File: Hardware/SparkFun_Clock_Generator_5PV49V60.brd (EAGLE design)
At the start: 27.9 x 25.4 mm, 74 parts, among them J1 QWIIC_RIGHT_ANGLE, J2 QWIIC_RIGHT_ANGLE, U1 IDT_5P49V60_CLOCK_GENERATOR, Y1 16MHz

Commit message: Update ferrite bead
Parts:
- FB1: value FERRITE_BEAD -> FERRITE_BEAD-120_OHM-0402
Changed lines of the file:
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@@
 <attribute name="VALUE" x="16.4846" y="10.033" size="0.6096" layer="27" font="vector" ratio="20" rot="R270" align="top-center"/>
 </element>
-<element name="FB1" library="SparkFun-Coils" package="0402" value="FERRITE_BEAD" x="18.6436" y="12.827" smashed="yes" rot="R180">
+<element name="FB1" library="SparkFun-Coils" package="0402" value="FERRITE_BEAD-120_OHM-0402" x="18.6436" y="12.827" smashed="yes" rot="R180">
+<attribute name="MFG_PART" value="BLM15HB121SN1D" x="18.6436" y="12.827" size="1.778" layer="27" rot="R180" display="off"/>
 <attribute name="NAME" x="18.6436" y="12.065" size="0.6096" layer="25" font="vector" ratio="20" rot="R180" align="bottom-center"/>
-<attribute name="VALUE" x="18.6436" y="13.589" size="0.6096" layer="27" font="vector" ratio="20" rot="R180" align="top-center"/>
+<attribute name="PROD_ID" value="NDUC-14206" x="18.6436" y="12.827" size="1.778" layer="27" rot="R180" display="off"/>
 </element>
 <element name="Y1" library="SparkFun-Clocks" package="CRYSTAL-SMD-2X2.5MM" value="16MHz" x="13.7414" y="19.0246" smashed="yes" rot="R180">

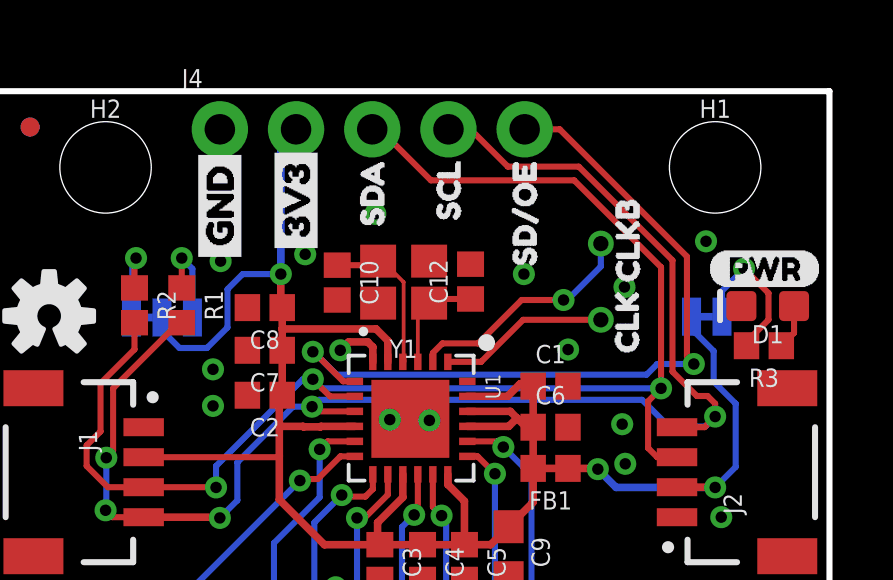
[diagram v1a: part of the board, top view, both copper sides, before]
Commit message: Updates crystal footprint, and fixes routing
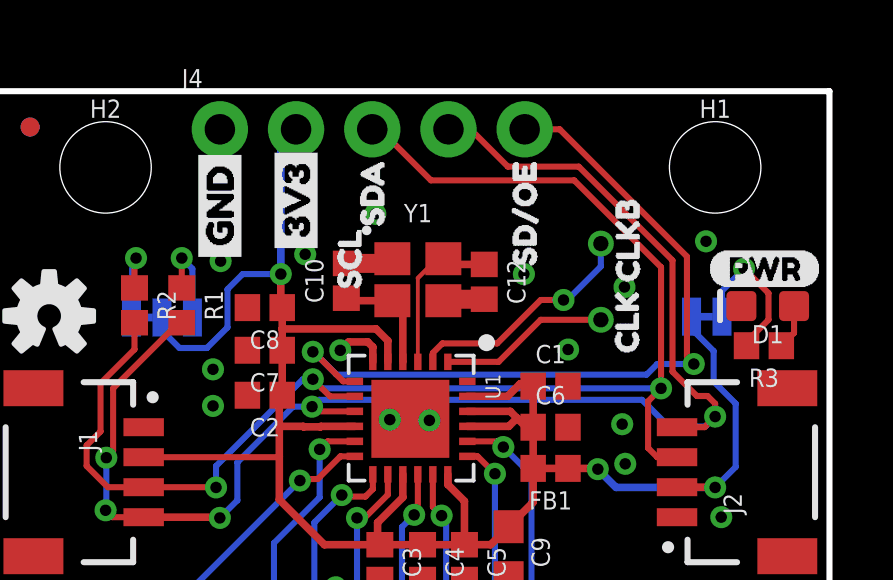
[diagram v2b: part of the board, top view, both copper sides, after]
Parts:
- moved U$6 4.02 mm to (11.9, 18.1)
- moved Y1 0.49 mm to (14.2, 19.1), turned to 0 degrees
- moved C12 0.46 mm to (16.4, 19.0), turned to 270 degrees
- moved C10 0.31 mm to (11.8, 19.1), turned to 90 degrees
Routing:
- net GND: track 42.4 -> 45.4 mm
- net N$2: track 3.55 -> 5.35 mm
- net N$6: track 5.23 -> 3.79 mm
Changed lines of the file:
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@@
 <layer number="37" name="tTest" color="7" fill="1" visible="no" active="yes"/>
 <layer number="38" name="bTest" color="7" fill="1" visible="no" active="yes"/>
-<layer number="39" name="tKeepout" color="4" fill="11" visible="no" active="yes"/>
+<layer number="39" name="tKeepout" color="4" fill="11" visible="yes" active="yes"/>
 <layer number="40" name="bKeepout" color="1" fill="11" visible="no" active="yes"/>
 <layer number="41" name="tRestrict" color="4" fill="10" visible="no" active="yes"/>
@@
 <attribute name="PROD_ID" value="NDUC-14206" x="18.6436" y="12.827" size="1.778" layer="27" rot="R180" display="off"/>
 </element>
-<element name="Y1" library="SparkFun-Clocks" package="CRYSTAL-SMD-2X2.5MM" value="16MHz" x="13.7414" y="19.0246" smashed="yes" rot="R180">
-<attribute name="NAME" x="13.7414" y="17.1196" size="0.6096" layer="25" font="vector" ratio="20" rot="R180" align="bottom-center"/>
-<attribute name="PROD_ID" value="XTAL-14664" x="13.7414" y="19.0246" size="1.778" layer="27" rot="R180" display="off"/>
-<attribute name="VALUE" value="16MHz" x="13.7414" y="19.0246" size="1.778" layer="27" rot="R180" display="off"/>
-</element>
-<element name="C12" library="SparkFun-Capacitors" package="0402" value="12pF" x="15.9766" y="19.0542" smashed="yes" rot="R90">
-<attribute name="NAME" x="15.2146" y="19.0542" size="0.6096" layer="25" font="vector" ratio="20" rot="R90" align="bottom-center"/>
-<attribute name="PROD_ID" value="CAP-14665" x="15.9766" y="19.0542" size="1.778" layer="27" font="vector" rot="R90" display="off"/>
-<attribute name="VALUE" value="12pF" x="16.7386" y="19.0542" size="0.6096" layer="27" font="vector" ratio="20" rot="R90" align="top-center"/>
-</element>
-<element name="C10" library="SparkFun-Capacitors" package="0402" value="12pF" x="11.5316" y="19.0204" smashed="yes" rot="R270">
-<attribute name="NAME" x="12.2936" y="19.0204" size="0.6096" layer="25" font="vector" ratio="20" rot="R270" align="bottom-center"/>
-<attribute name="PROD_ID" value="CAP-14665" x="11.5316" y="19.0204" size="1.778" layer="27" font="vector" rot="R270" display="off"/>
-<attribute name="VALUE" value="12pF" x="10.7696" y="19.0204" size="0.6096" layer="27" font="vector" ratio="20" rot="R270" align="top-center"/>
+<element name="Y1" library="SparkFun-Clocks" package="CRYSTAL-SMD-2X2.5MM" value="16MHz" x="14.224" y="19.1262" smashed="yes">
+<attribute name="NAME" x="14.224" y="21.0312" size="0.6096" layer="25" font="vector" ratio="20" align="bottom-center"/>
+<attribute name="PROD_ID" value="XTAL-14664" x="14.224" y="19.1262" size="1.778" layer="27" display="off"/>
+<attribute name="VALUE" value="16MHz" x="14.224" y="19.1262" size="1.778" layer="27" display="off"/>
+</element>
+<element name="C12" library="SparkFun-Capacitors" package="0402" value="12pF" x="16.4338" y="19.0458" smashed="yes" rot="R270">
+<attribute name="NAME" x="17.1958" y="19.0458" size="0.6096" layer="25" font="vector" ratio="20" rot="R270" align="bottom-center"/>
+<attribute name="PROD_ID" value="CAP-14665" x="16.4338" y="19.0458" size="1.778" layer="27" font="vector" rot="R270" display="off"/>
+<attribute name="VALUE" value="12pF" x="15.6718" y="19.0458" size="0.6096" layer="27" font="vector" ratio="20" rot="R270" align="top-center"/>
+</element>
+<element name="C10" library="SparkFun-Capacitors" package="0402" value="12pF" x="11.8364" y="19.0796" smashed="yes" rot="R90">
+<attribute name="NAME" x="11.0744" y="19.0796" size="0.6096" layer="25" font="vector" ratio="20" rot="R90" align="bottom-center"/>
+<attribute name="PROD_ID" value="CAP-14665" x="11.8364" y="19.0796" size="1.778" layer="27" font="vector" rot="R90" display="off"/>
+<attribute name="VALUE" value="12pF" x="12.5984" y="19.0796" size="0.6096" layer="27" font="vector" ratio="20" rot="R90" align="top-center"/>
 </element>
 <element name="D1" library="SparkFun-LED" package="LED-0603" value="RED" x="25.8826" y="18.2372" smashed="yes" rot="R180">
@@
 <element name="U$4" library="Labels" package="PWR-()-03" value="" x="23.9014" y="19.4818" smashed="yes"/>
 <element name="U$5" library="Every Label" package="SDA11" value="" x="12.7" y="20.2184" smashed="yes" rot="R90"/>
-<element name="U$6" library="Every Label" package="SCL10" value="" x="15.24" y="20.4216" smashed="yes" rot="R90"/>
+<element name="U$6" library="Every Label" package="SCL10" value="" x="11.938" y="18.1356" smashed="yes" rot="R90"/>
 <element name="U$7" library="Every Label" package="SD#OE12" value="" x="17.78" y="18.8976" smashed="yes" rot="R90"/>
 <element name="U$16" library="Every Label" package="CLOCK_GENERATOR0" value="" x="20.447" y="13.2842" smashed="yes" rot="MR0"/>
@@
 <wire x1="11.9126" y1="17.0434" x2="11.6332" y2="16.764" width="0.254" layer="1"/>
 <via x="23.8252" y="20.3962" extent="1-16" drill="0.381"/>
-<contactref element="Y1" pad="P2"/>
-<contactref element="Y1" pad="P4"/>
-<contactref element="C10" pad="2"/>
-<contactref element="C12" pad="2"/>
 <contactref element="D1" pad="C"/>
 <via x="7.8486" y="8.2296" extent="1-16" drill="0.381"/>
@@
 <via x="19.2278" y="16.7894" extent="1-16" drill="0.381"/>
 <via x="10.4648" y="19.9644" extent="1-16" drill="0.381"/>
+<contactref element="Y1" pad="P2"/>
+<contactref element="Y1" pad="P4"/>
+<contactref element="C10" pad="2"/>
+<contactref element="C12" pad="2"/>
+<wire x1="13.37" y1="19.8162" x2="13.2134" y2="19.6596" width="0.635" layer="1"/>
+<wire x1="13.2134" y1="19.6596" x2="11.8364" y2="19.6596" width="0.635" layer="1"/>
+<wire x1="15.07" y1="18.4162" x2="15.1196" y2="18.4658" width="0.635" layer="1"/>
+<wire x1="15.1196" y1="18.4658" x2="16.4338" y2="18.4658" width="0.635" layer="1"/>
 </signal>
 <signal name="3.3V">
@@
 <signal name="CLKIN">
 <contactref element="U1" pad="P1"/>
-<wire x1="15.22" y1="16.378" x2="16.3272" y2="16.378" width="0.2032" layer="1"/>
-<wire x1="16.3272" y1="16.378" x2="17.7292" y2="17.78" width="0.2032" layer="1"/>
+<wire x1="15.22" y1="16.378" x2="16.9114" y2="16.378" width="0.2032" layer="1"/>
+<wire x1="16.9114" y1="16.378" x2="18.3134" y2="17.78" width="0.2032" layer="1"/>
 <contactref element="J8" pad="P$1"/>
-<wire x1="17.7292" y1="17.78" x2="20.32" y2="17.78" width="0.2032" layer="1"/>
+<wire x1="18.3134" y1="17.78" x2="20.32" y2="17.78" width="0.2032" layer="1"/>
 </signal>
 <signal name="CLKINB">
 <contactref element="U1" pad="P2"/>
-<wire x1="15.0368" y1="16.9926" x2="16.2306" y2="16.9926" width="0.2032" layer="1"/>
+<wire x1="15.0368" y1="16.9926" x2="16.8656" y2="16.9926" width="0.2032" layer="1"/>
 <wire x1="14.72" y1="16.6758" x2="14.72" y2="16.378" width="0.2032" layer="1"/>
 <wire x1="15.0368" y1="16.9926" x2="14.72" y2="16.6758" width="0.2032" layer="1"/>
 <contactref element="J7" pad="P$1"/>
-<wire x1="16.2306" y1="16.9926" x2="17.6784" y2="18.4404" width="0.2032" layer="1"/>
-<wire x1="17.6784" y1="18.4404" x2="19.0754" y2="18.4404" width="0.2032" layer="1"/>
+<wire x1="16.8656" y1="16.9926" x2="18.3134" y2="18.4404" width="0.2032" layer="1"/>
+<wire x1="18.3134" y1="18.4404" x2="19.0754" y2="18.4404" width="0.2032" layer="1"/>
 <via x="19.0754" y="18.4404" extent="1-16" drill="0.381"/>
 <wire x1="20.32" y1="20.32" x2="20.32" y2="19.558" width="0.2032" layer="16"/>
@@
 <signal name="N$6">
 <contactref element="U1" pad="P4"/>
+<contactref element="C10" pad="1"/>
+<wire x1="13.72" y1="16.378" x2="13.7454" y2="16.4034" width="0.2032" layer="1"/>
 <contactref element="Y1" pad="P3"/>
-<contactref element="C10" pad="1"/>
-<wire x1="13.7454" y1="19.037" x2="13.0478" y2="19.7346" width="0.127" layer="1"/>
-<wire x1="13.0478" y1="19.7346" x2="12.8954" y2="19.7346" width="0.2032" layer="1"/>
-<wire x1="13.72" y1="16.378" x2="13.7454" y2="16.4034" width="0.2032" layer="1"/>
-<wire x1="13.7454" y1="19.037" x2="13.7454" y2="16.4034" width="0.127" layer="1"/>
-<wire x1="12.8954" y1="19.7346" x2="12.7612" y2="19.6004" width="0.2032" layer="1"/>
-<wire x1="12.7612" y1="19.6004" x2="11.5316" y2="19.6004" width="0.2032" layer="1"/>
+<wire x1="13.72" y1="16.378" x2="13.72" y2="18.0662" width="0.254" layer="1"/>
+<wire x1="13.72" y1="18.0662" x2="13.37" y2="18.4162" width="0.254" layer="1"/>
+<wire x1="13.37" y1="18.4162" x2="11.9198" y2="18.4162" width="0.254" layer="1"/>
+<wire x1="11.9198" y1="18.4162" x2="11.8364" y2="18.4996" width="0.254" layer="1"/>
 </signal>
 <signal name="N$2">
 <contactref element="U1" pad="P3"/>
+<contactref element="C12" pad="1"/>
 <contactref element="Y1" pad="P1"/>
-<contactref element="C12" pad="1"/>
-<wire x1="14.22" y1="16.378" x2="14.22" y2="17.9592" width="0.127" layer="1"/>
-<wire x1="14.22" y1="17.9592" x2="14.5954" y2="18.3346" width="0.2032" layer="1"/>
-<wire x1="14.5954" y1="18.3346" x2="14.735" y2="18.4742" width="0.2032" layer="1"/>
-<wire x1="14.735" y1="18.4742" x2="15.9766" y2="18.4742" width="0.2032" layer="1"/>
+<wire x1="14.22" y1="16.378" x2="14.22" y2="19.1694" width="0.127" layer="1"/>
+<wire x1="14.8668" y1="19.8162" x2="14.22" y2="19.1694" width="0.1524" layer="1"/>
+<wire x1="14.8668" y1="19.8162" x2="15.07" y2="19.8162" width="0.1524" layer="1"/>
+<wire x1="16.4338" y1="19.6258" x2="15.2604" y2="19.6258" width="0.254" layer="1"/>
+<wire x1="15.2604" y1="19.6258" x2="15.07" y2="19.8162" width="0.254" layer="1"/>
 </signal>
 <signal name="N$4">

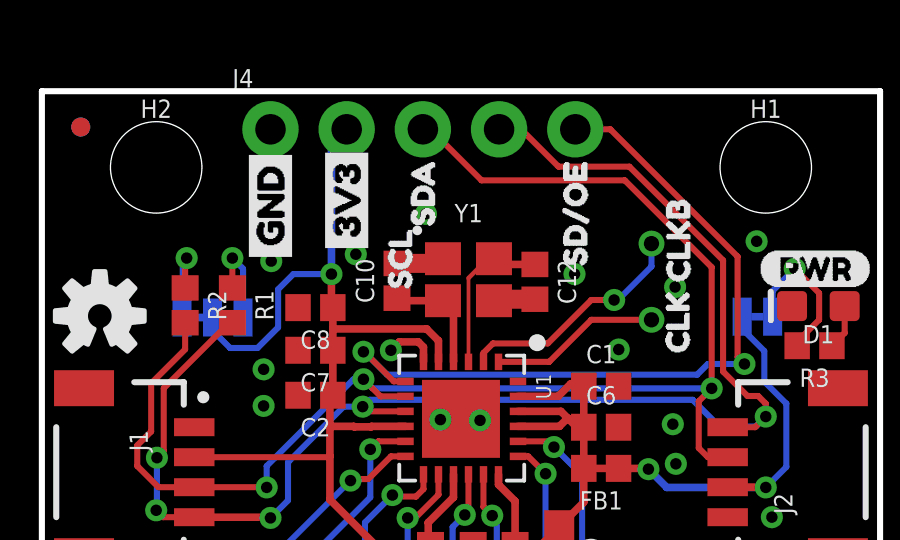
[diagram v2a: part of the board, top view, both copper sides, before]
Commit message: Moves SCL silk back to its' pin
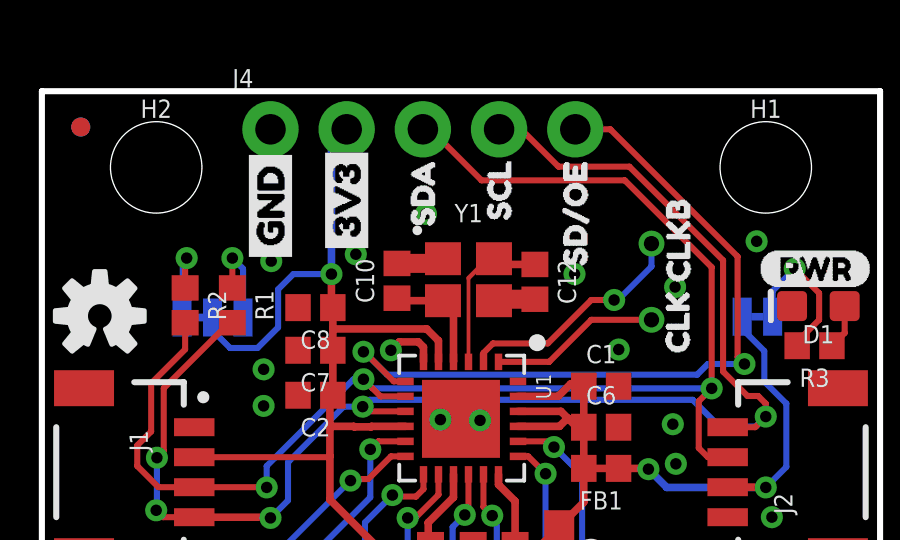
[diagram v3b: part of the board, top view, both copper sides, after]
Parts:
- moved U$6 4.02 mm to (15.2, 20.4)
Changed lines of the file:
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@@
 <element name="U$4" library="Labels" package="PWR-()-03" value="" x="23.9014" y="19.4818" smashed="yes"/>
 <element name="U$5" library="Every Label" package="SDA11" value="" x="12.7" y="20.2184" smashed="yes" rot="R90"/>
-<element name="U$6" library="Every Label" package="SCL10" value="" x="11.938" y="18.1356" smashed="yes" rot="R90"/>
+<element name="U$6" library="Every Label" package="SCL10" value="" x="15.24" y="20.4216" smashed="yes" rot="R90"/>
 <element name="U$7" library="Every Label" package="SD#OE12" value="" x="17.78" y="18.8976" smashed="yes" rot="R90"/>
 <element name="U$16" library="Every Label" package="CLOCK_GENERATOR0" value="" x="20.447" y="13.2842" smashed="yes" rot="MR0"/>

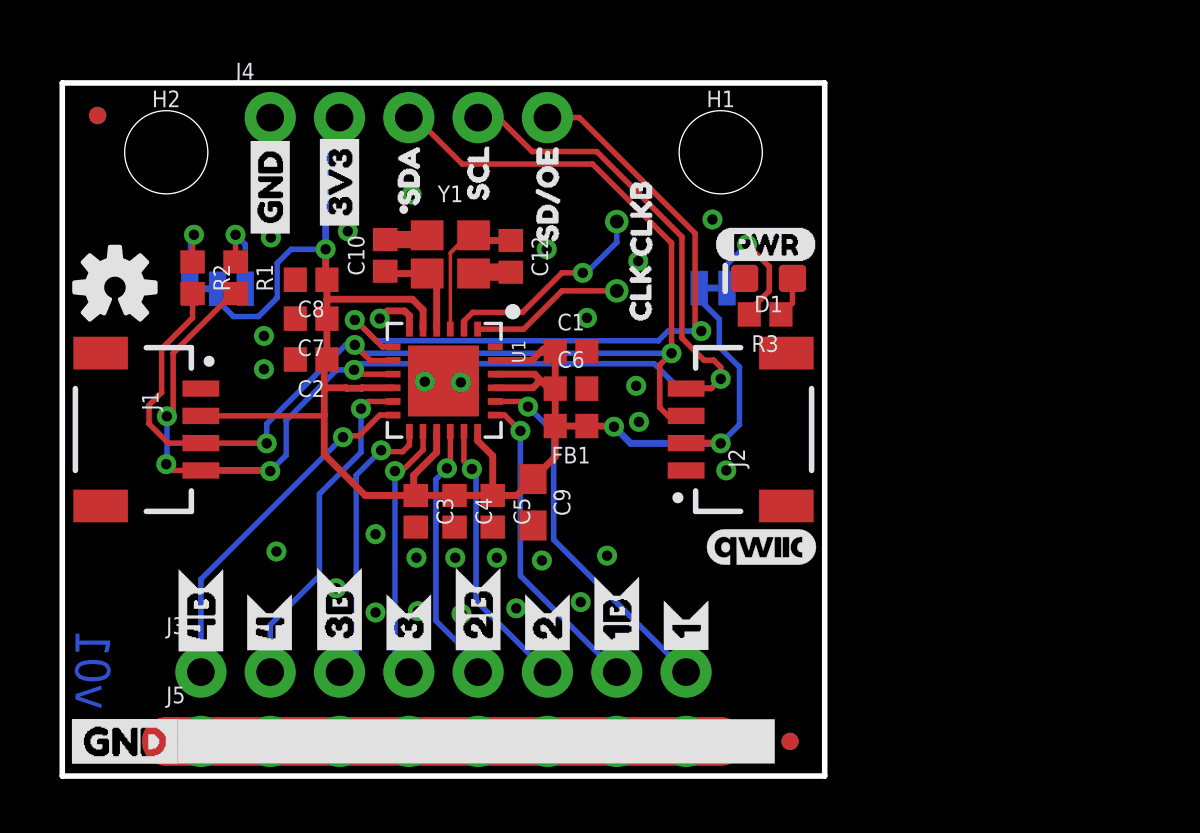
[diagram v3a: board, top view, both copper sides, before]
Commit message: Radical change to design
* Moved all parts besides crystal and IC to "bottom of board"
  * This allows for better routing of Clock signals
* Adds 2.2Ohm series resistor to power rail
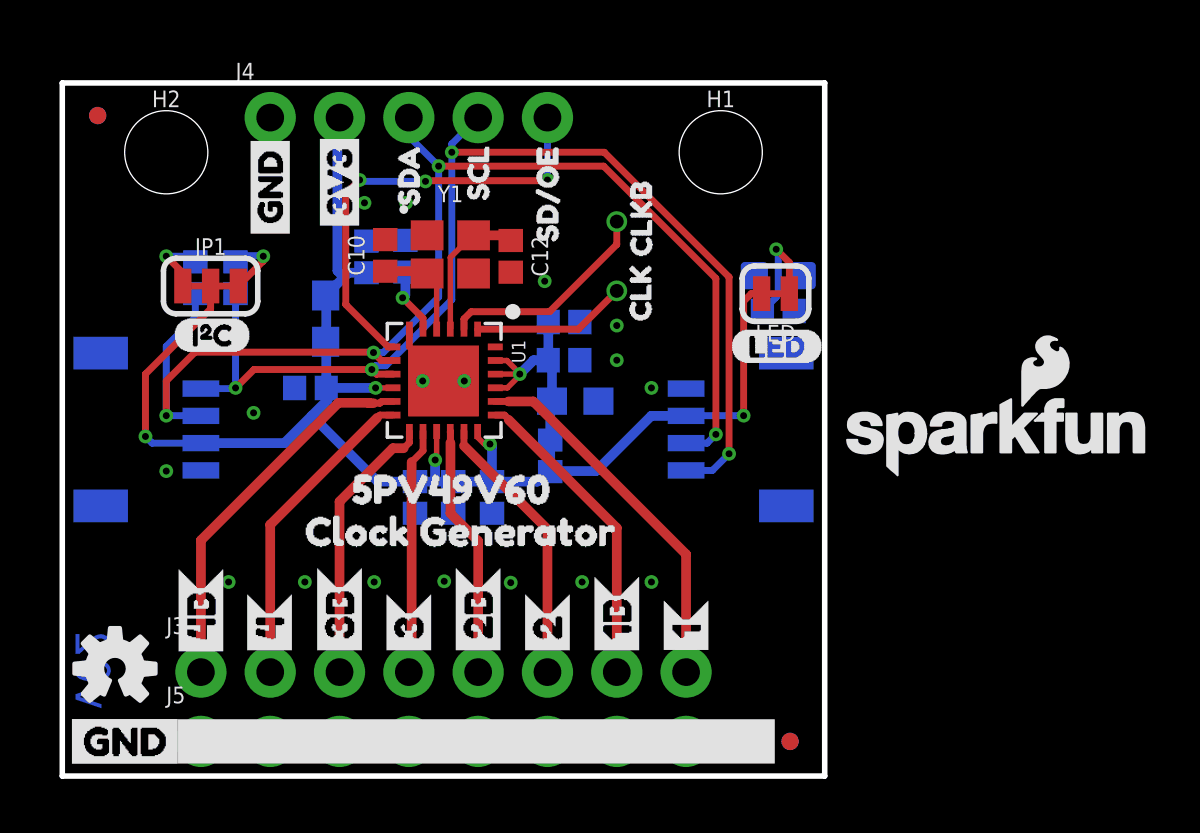
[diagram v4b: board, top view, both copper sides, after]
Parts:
- added R4: 2.2, SparkFun-Resistors:0603
- moved LOGO1 20.5 mm to (34.3, 12.4), flipped to the top
- moved LOGO2 14.0 mm to (1.93, 3.94)
- moved U$16 13.2 mm to (8.00, 8.97), flipped to the top
- moved U$17 9.10 mm to (9.70, 10.5), flipped to the top
- moved C2 5.12 mm to (12.6, 19.1), flipped to the bottom, turned to 90 degrees
- moved C9 4.02 mm to (18.8, 13.7), flipped to the bottom, turned to 180 degrees
- moved U$35 2.98 mm to (4.06, 16.2), flipped to the top
- moved C5 2.89 mm to (12.9, 10.2), flipped to the bottom
- moved C3 2.84 mm to (15.7, 10.2), flipped to the bottom
- moved C7 2.54 mm to (9.09, 14.2), flipped to the bottom, turned to 0 degrees
- moved LED 2.30 mm to (26.1, 17.7), flipped to the top, turned to 180 degrees
- moved C8 2.20 mm to (11.2, 19.0), flipped to the bottom, turned to 90 degrees
- moved FB1 1.33 mm to (17.9, 11.7), flipped to the bottom, turned to 90 degrees
- moved U$36 1.15 mm to (24.5, 15.7), flipped to the top
- moved C1 1.10 mm to (18.4, 16.6), flipped to the bottom, turned to 180 degrees
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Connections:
- net 3.3V: now also R4.1, R4.2
- net OUT4: now also U1.P12; no longer U1.P11
- net OUT4B: now also U1.P11; no longer U1.P12
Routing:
- net GND: track 45.4 -> 0.65 mm, vias 28 -> 17
- net SD/OE: track 25.8 -> 16.4 mm, vias 2 -> 3
- net SEL0/SCL: track 48.9 -> 42.3 mm, vias 5 -> 4
- net SEL1/SDA: track 47.4 -> 45.4 mm, vias 3 -> 4
- net 3.3V: track 70.3 -> 69.1 mm, vias 3 -> 7
- net OUT4B: track 13.0 -> 14.0 mm, vias 1 -> 0
- net N$4: track 5.11 -> 4.36 mm
- net OUT4: track 12.3 -> 11.6 mm, vias 1 -> 0
- net OUT3: track 9.60 -> 9.03 mm, vias 1 -> 0
- net N$1: track 3.06 -> 2.50 mm
- net N$3: track 3.12 -> 2.59 mm
- net OUT2B: track 9.68 -> 9.24 mm, vias 1 -> 0
- net OUT3B: track 10.4 -> 10.1 mm, vias 1 -> 0
- net OUT1: track 13.4 -> 13.6 mm, vias 1 -> 0
- net CLKINB: track 7.85 -> 7.94 mm, vias 1 -> 0
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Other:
- board text added: "v02"
- board text removed: "v01"
